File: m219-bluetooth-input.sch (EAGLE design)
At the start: 68 parts, among them U1 SCREW-M2X8, U10 FX2-20S-1.27DS, U2 SCREW-M2X8, U3 NUT-M2-SELFLOCK, U4 NUT-M2-SELFLOCK, U5 FX2-20P-1.27DS, U6 SCREW-M2X8, U7 SCREW-M2X8, U8 NUT-M2-SELFLOCK, U9 NUT-M2-SELFLOCK

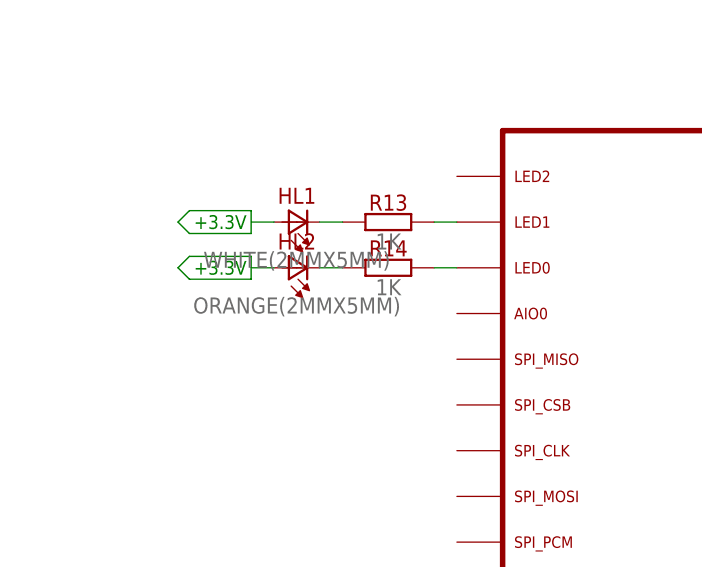
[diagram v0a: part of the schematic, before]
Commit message: M219 LED Color Update
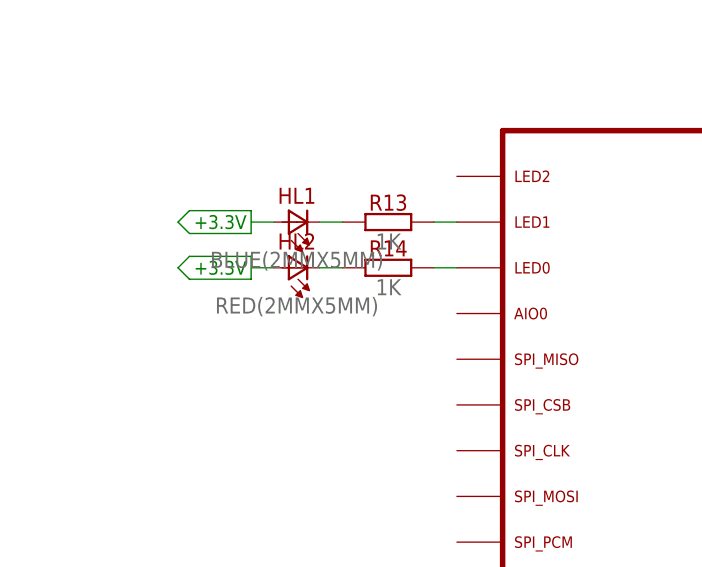
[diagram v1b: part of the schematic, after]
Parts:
- HL1: value WHITE(2MMX5MM) -> BLUE(2MMX5MM); device optoelectronics:WHITE(2MMX5MM) -> optoelectronics:BLUE(2MMX5MM)
- HL2: value ORANGE(2MMX5MM) -> RED(2MMX5MM); device optoelectronics:ORANGE(2MMX5MM) -> optoelectronics:RED(2MMX5MM)
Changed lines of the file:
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@@
 <part name="R13" library="resistors" deviceset="?" device="1K"/>
 <part name="R14" library="resistors" deviceset="?" device="1K"/>
-<part name="HL2" library="optoelectronics" deviceset="?(2MMX5MM)" device="ORANGE"/>
-<part name="HL1" library="optoelectronics" deviceset="?(2MMX5MM)" device="WHITE"/>
+<part name="HL2" library="optoelectronics" deviceset="?(2MMX5MM)" device="RED" value="RED(2MMX5MM)"/>
+<part name="HL1" library="optoelectronics" deviceset="?(2MMX5MM)" device="BLUE" value="BLUE(2MMX5MM)"/>
 <part name="PWR1" library="supply" deviceset="+3.3V" device=""/>
 <part name="PWR2" library="supply" deviceset="+3.3V" device=""/>

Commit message: M219a Routing
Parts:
- HL1: value BLUE(2MMX5MM) -> GREEN(2MMX5MM); device optoelectronics:BLUE(2MMX5MM) -> optoelectronics:GREEN(2MMX5MM)
- HL2: value RED(2MMX5MM) -> YELLOW(2MMX5MM); device optoelectronics:RED(2MMX5MM) -> optoelectronics:YELLOW(2MMX5MM)
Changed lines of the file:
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@@
 <part name="R13" library="resistors" deviceset="?" device="1K"/>
 <part name="R14" library="resistors" deviceset="?" device="1K"/>
-<part name="HL2" library="optoelectronics" deviceset="?(2MMX5MM)" device="RED" value="RED(2MMX5MM)"/>
-<part name="HL1" library="optoelectronics" deviceset="?(2MMX5MM)" device="BLUE" value="BLUE(2MMX5MM)"/>
+<part name="HL2" library="optoelectronics" deviceset="?(2MMX5MM)" device="YELLOW" value="YELLOW(2MMX5MM)"/>
+<part name="HL1" library="optoelectronics" deviceset="?(2MMX5MM)" device="GREEN" value="GREEN(2MMX5MM)"/>
 <part name="PWR1" library="supply" deviceset="+3.3V" device=""/>
 <part name="PWR2" library="supply" deviceset="+3.3V" device=""/>
